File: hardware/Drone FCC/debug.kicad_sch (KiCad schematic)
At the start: 1 part, among them J601 SWD Debug Connector

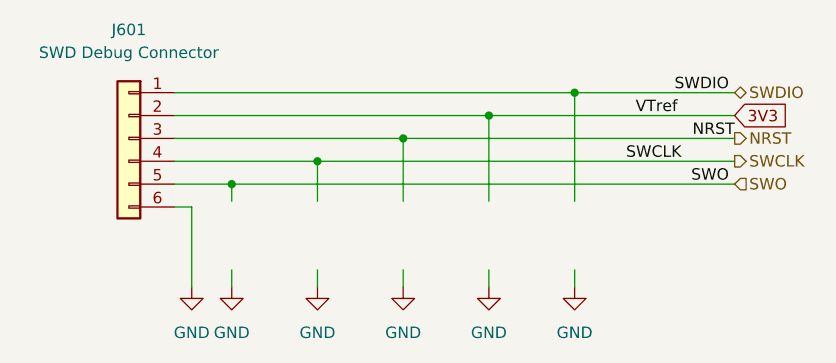
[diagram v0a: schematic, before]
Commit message: tidying up the schematic
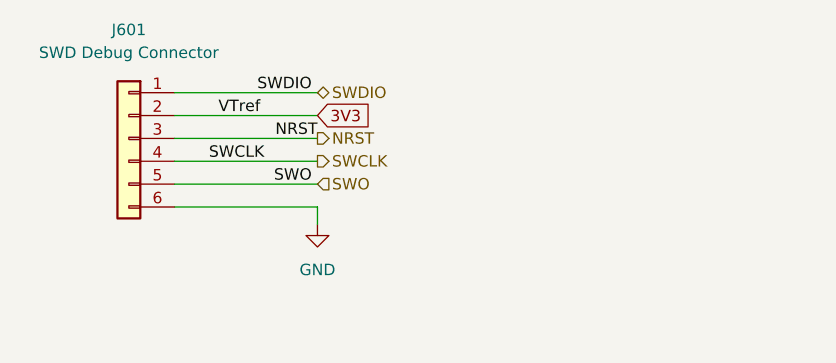
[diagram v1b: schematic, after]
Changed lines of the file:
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@@
 (kicad_sch (version 20211123) (generator eeschema)
   (paper "A4")
-  (junction (at 160.02 80.01) (diameter 0) (color 0 0 0 0)
-  )
-  (junction (at 140.97 85.09) (diameter 0) (color 0 0 0 0)
-  )
-  (junction (at 131.445 87.63) (diameter 0) (color 0 0 0 0)
-  )
-  (junction (at 169.545 77.47) (diameter 0) (color 0 0 0 0)
-  )
-  (junction (at 150.495 82.55) (diameter 0) (color 0 0 0 0)
-  )
-  (wire (pts (xy 140.97 97.155) (xy 140.97 99.06))
+  (wire (pts (xy 125.095 82.55) (xy 140.97 82.55))
     (stroke (width 0) (type default) (color 0 0 0 0))
   )
-  (wire (pts (xy 140.97 85.09) (xy 187.325 85.09))
+  (wire (pts (xy 140.97 90.17) (xy 140.97 92.075))
     (stroke (width 0) (type default) (color 0 0 0 0))
   )
-  (wire (pts (xy 131.445 87.63) (xy 187.325 87.63))
+  (wire (pts (xy 125.095 87.63) (xy 140.97 87.63))
     (stroke (width 0) (type default) (color 0 0 0 0))
   )
-  (wire (pts (xy 131.445 97.155) (xy 131.445 99.06))
+  (wire (pts (xy 125.095 80.01) (xy 140.97 80.01))
     (stroke (width 0) (type default) (color 0 0 0 0))
   )
-  (wire (pts (xy 150.495 82.55) (xy 187.325 82.55))
+  (wire (pts (xy 125.095 90.17) (xy 140.97 90.17))
+    (stroke (width 0) (type default) (color 0 0 0 0))
+  )
+  (wire (pts (xy 125.095 77.47) (xy 140.97 77.47))
     (stroke (width 0) (type default) (color 0 0 0 0))
   )
@@
     (stroke (width 0) (type default) (color 0 0 0 0))
   )
-  (wire (pts (xy 169.545 77.47) (xy 169.545 89.535))
-    (stroke (width 0) (type default) (color 0 0 0 0))
-  )
-  (wire (pts (xy 127 90.17) (xy 127 99.06))
-    (stroke (width 0) (type default) (color 0 0 0 0))
-  )
-  (wire (pts (xy 150.495 82.55) (xy 150.495 89.535))
-    (stroke (width 0) (type default) (color 0 0 0 0))
-  )
-  (wire (pts (xy 125.095 80.01) (xy 160.02 80.01))
-    (stroke (width 0) (type default) (color 0 0 0 0))
-  )
-  (wire (pts (xy 125.095 90.17) (xy 127 90.17))
-    (stroke (width 0) (type default) (color 0 0 0 0))
-  )
-  (wire (pts (xy 160.02 80.01) (xy 160.02 89.535))
-    (stroke (width 0) (type default) (color 0 0 0 0))
-  )
-  (wire (pts (xy 169.545 77.47) (xy 187.325 77.47))
-    (stroke (width 0) (type default) (color 0 0 0 0))
-  )
-  (wire (pts (xy 150.495 82.55) (xy 125.095 82.55))
-    (stroke (width 0) (type default) (color 0 0 0 0))
-  )
-  (wire (pts (xy 125.095 77.47) (xy 169.545 77.47))
-    (stroke (width 0) (type default) (color 0 0 0 0))
-  )
-  (wire (pts (xy 160.02 80.01) (xy 187.325 80.01))
-    (stroke (width 0) (type default) (color 0 0 0 0))
-  )
-  (wire (pts (xy 140.97 85.09) (xy 140.97 89.535))
-    (stroke (width 0) (type default) (color 0 0 0 0))
-  )
-  (wire (pts (xy 160.02 97.155) (xy 160.02 99.06))
-    (stroke (width 0) (type default) (color 0 0 0 0))
-  )
-  (wire (pts (xy 169.545 97.155) (xy 169.545 99.06))
-    (stroke (width 0) (type default) (color 0 0 0 0))
-  )
-  (wire (pts (xy 131.445 87.63) (xy 131.445 89.535))
-    (stroke (width 0) (type default) (color 0 0 0 0))
-  )
-  (wire (pts (xy 125.095 87.63) (xy 131.445 87.63))
-    (stroke (width 0) (type default) (color 0 0 0 0))
-  )
-  (wire (pts (xy 150.495 97.155) (xy 150.495 99.06))
-    (stroke (width 0) (type default) (color 0 0 0 0))
-  )
-  (label "SWDIO" (at 186.69 77.47 180)
+  (label "SWDIO" (at 140.335 77.47 180)
     (effects (font (size 1.27 1.27)) (justify right bottom))
   )
-  (label "VTref" (at 180.975 80.01 180)
+  (label "VTref" (at 134.62 80.01 180)
     (effects (font (size 1.27 1.27)) (justify right bottom))
   )
-  (label "SWCLK" (at 175.26 85.09 0)
+  (label "SWCLK" (at 128.905 85.09 0)
     (effects (font (size 1.27 1.27)) (justify left bottom))
   )
-  (label "NRST" (at 187.325 82.55 180)
+  (label "NRST" (at 140.97 82.55 180)
     (effects (font (size 1.27 1.27)) (justify right bottom))
   )
-  (label "SWO" (at 186.69 87.63 180)
+  (label "SWO" (at 140.335 87.63 180)
     (effects (font (size 1.27 1.27)) (justify right bottom))
   )
-  (global_label "3V3" (shape input) (at 187.325 80.01 0) (fields_autoplaced)
+  (global_label "3V3" (shape input) (at 140.97 80.01 0) (fields_autoplaced)
     (effects (font (size 1.27 1.27)) (justify left))
-    (property "Intersheet References" "${INTERSHEET_REFS}" (id 0) (at 193.2457 80.0894 0)
+    (property "Intersheet References" "${INTERSHEET_REFS}" (id 0) (at 146.8907 80.0894 0)
       (effects (font (size 1.27 1.27)) (justify left) hide)
     )
   )
-  (hierarchical_label "SWCLK" (shape output) (at 187.325 85.09 0)
+  (hierarchical_label "SWCLK" (shape output) (at 140.97 85.09 0)
     (effects (font (size 1.27 1.27)) (justify left))
   )
-  (hierarchical_label "NRST" (shape output) (at 187.325 82.55 0)
+  (hierarchical_label "NRST" (shape output) (at 140.97 82.55 0)
     (effects (font (size 1.27 1.27)) (justify left))
   )
-  (hierarchical_label "SWO" (shape input) (at 187.325 87.63 0)
+  (hierarchical_label "SWO" (shape input) (at 140.97 87.63 0)
     (effects (font (size 1.27 1.27)) (justify left))
   )
-  (hierarchical_label "SWDIO" (shape bidirectional) (at 187.325 77.47 0)
+  (hierarchical_label "SWDIO" (shape bidirectional) (at 140.97 77.47 0)
     (effects (font (size 1.27 1.27)) (justify left))
   )
-  (symbol (lib_id "power:GND") (at 131.445 99.06 0) (mirror y) (unit 1)
+  (symbol (lib_id "power:GND") (at 140.97 92.075 0) (mirror y) (unit 1)
     (in_bom yes) (on_board yes) (fields_autoplaced)
-    (property "Reference" "#PWR0222" (id 0) (at 131.445 105.41 0)
+    (property "Reference" "#PWR0118" (id 0) (at 140.97 98.425 0)
       (effects (font (size 1.27 1.27)) hide)
     )
-    (property "Value" "GND" (id 1) (at 131.445 104.14 0))
-    (property "Footprint" "" (id 2) (at 131.445 99.06 0)
+    (property "Value" "GND" (id 1) (at 140.97 97.155 0))
+    (property "Footprint" "" (id 2) (at 140.97 92.075 0)
       (effects (font (size 1.27 1.27)) hide)
     )
-    (property "Datasheet" "" (id 3) (at 131.445 99.06 0)
-      (effects (font (size 1.27 1.27)) hide)
-    )
-    (pin "1")
-  )
-  (symbol (lib_id "power:GND") (at 160.02 99.06 0) (mirror y) (unit 1)
-    (in_bom yes) (on_board yes) (fields_autoplaced)
-    (property "Reference" "#PWR0221" (id 0) (at 160.02 105.41 0)
-      (effects (font (size 1.27 1.27)) hide)
-    )
-    (property "Value" "GND" (id 1) (at 160.02 104.14 0))
-    (property "Footprint" "" (id 2) (at 160.02 99.06 0)
-      (effects (font (size 1.27 1.27)) hide)
-    )
-    (property "Datasheet" "" (id 3) (at 160.02 99.06 0)
-      (effects (font (size 1.27 1.27)) hide)
-    )
-    (pin "1")
-  )
-  (symbol (lib_id "power:GND") (at 140.97 99.06 0) (mirror y) (unit 1)
-    (in_bom yes) (on_board yes) (fields_autoplaced)
-    (property "Reference" "#PWR0220" (id 0) (at 140.97 105.41 0)
-      (effects (font (size 1.27 1.27)) hide)
-    )
-    (property "Value" "GND" (id 1) (at 140.97 104.14 0))
-    (property "Footprint" "" (id 2) (at 140.97 99.06 0)
-      (effects (font (size 1.27 1.27)) hide)
-    )
-    (property "Datasheet" "" (id 3) (at 140.97 99.06 0)
-      (effects (font (size 1.27 1.27)) hide)
-    )
-    (pin "1")
-  )
-  (symbol (lib_id "power:GND") (at 127 99.06 0) (mirror y) (unit 1)
-    (in_bom yes) (on_board yes) (fields_autoplaced)
-    (property "Reference" "#PWR0118" (id 0) (at 127 105.41 0)
-      (effects (font (size 1.27 1.27)) hide)
-    )
-    (property "Value" "GND" (id 1) (at 127 104.14 0))
-    (property "Footprint" "" (id 2) (at 127 99.06 0)
-      (effects (font (size 1.27 1.27)) hide)
-    )
-    (property "Datasheet" "" (id 3) (at 127 99.06 0)
-      (effects (font (size 1.27 1.27)) hide)
-    )
-    (pin "1")
-  )
-  (symbol (lib_id "power:GND") (at 169.545 99.06 0) (mirror y) (unit 1)
-    (in_bom yes) (on_board yes) (fields_autoplaced)
-    (property "Reference" "#PWR0218" (id 0) (at 169.545 105.41 0)
-      (effects (font (size 1.27 1.27)) hide)
-    )
-    (property "Value" "GND" (id 1) (at 169.545 104.14 0))
-    (property "Footprint" "" (id 2) (at 169.545 99.06 0)
-      (effects (font (size 1.27 1.27)) hide)
-    )
-    (property "Datasheet" "" (id 3) (at 169.545 99.06 0)
+    (property "Datasheet" "" (id 3) (at 140.97 92.075 0)
       (effects (font (size 1.27 1.27)) hide)
     )
@@
     (pin "6")
   )
-  (symbol (lib_id "power:GND") (at 150.495 99.06 0) (mirror y) (unit 1)
-    (in_bom yes) (on_board yes) (fields_autoplaced)
-    (property "Reference" "#PWR0219" (id 0) (at 150.495 105.41 0)
-      (effects (font (size 1.27 1.27)) hide)
-    )
-    (property "Value" "GND" (id 1) (at 150.495 104.14 0))
-    (property "Footprint" "" (id 2) (at 150.495 99.06 0)
-      (effects (font (size 1.27 1.27)) hide)
-    )
-    (property "Datasheet" "" (id 3) (at 150.495 99.06 0)
-      (effects (font (size 1.27 1.27)) hide)
-    )
-    (pin "1")
-  )
 )

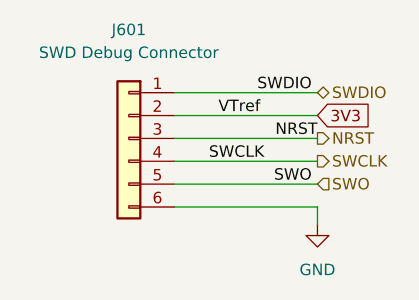
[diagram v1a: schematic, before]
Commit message: re enumeation of componentes
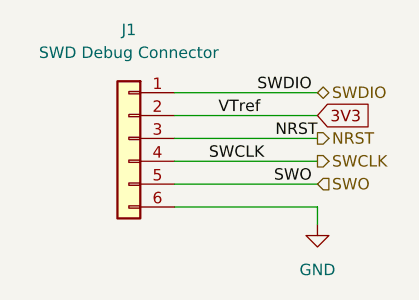
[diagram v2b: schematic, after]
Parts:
- renumbered J601 to J1
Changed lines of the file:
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@@
   (symbol (lib_id "power:GND") (at 140.97 92.075 0) (mirror y) (unit 1)
     (in_bom yes) (on_board yes) (fields_autoplaced)
-    (property "Reference" "#PWR0118" (id 0) (at 140.97 98.425 0)
+    (property "Reference" "#PWR05" (id 0) (at 140.97 98.425 0)
       (effects (font (size 1.27 1.27)) hide)
     )
@@
   (symbol (lib_id "Connector_Generic:Conn_01x06") (at 120.015 82.55 0) (mirror y) (unit 1)
     (in_bom yes) (on_board yes) (fields_autoplaced)
-    (property "Reference" "J601" (id 0) (at 120.015 70.485 0))
+    (property "Reference" "J1" (id 0) (at 120.015 70.485 0))
     (property "Value" "SWD Debug Connector" (id 1) (at 120.015 73.025 0))
     (property "Footprint" "Connector_PinHeader_2.54mm:PinHeader_2x03_P2.54mm_Vertical" (id 2) (at 120.015 82.55 0)
